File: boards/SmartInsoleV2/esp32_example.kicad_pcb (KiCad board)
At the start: 2 copper layers, 49 x 38.4 mm, 49 parts, among them J1 Conn_01x02_Pin, J2 USB_B_Micro, J3 Conn_01x05_Female, J4 Conn_02x10_Odd_Even, J5 Conn_01x02_Pin, J7 Conn_ARM_JTAG_SWD_10, J8 Conn_01x02_Pin, Q2 SS8050-G, Q3 SS8050-G, SW1 SW_Push, SW2 SW_Push, U1 MPU-6050, U3 TLV75801PDRV, U7 ESP32-S3-WROOM-1-N16R2

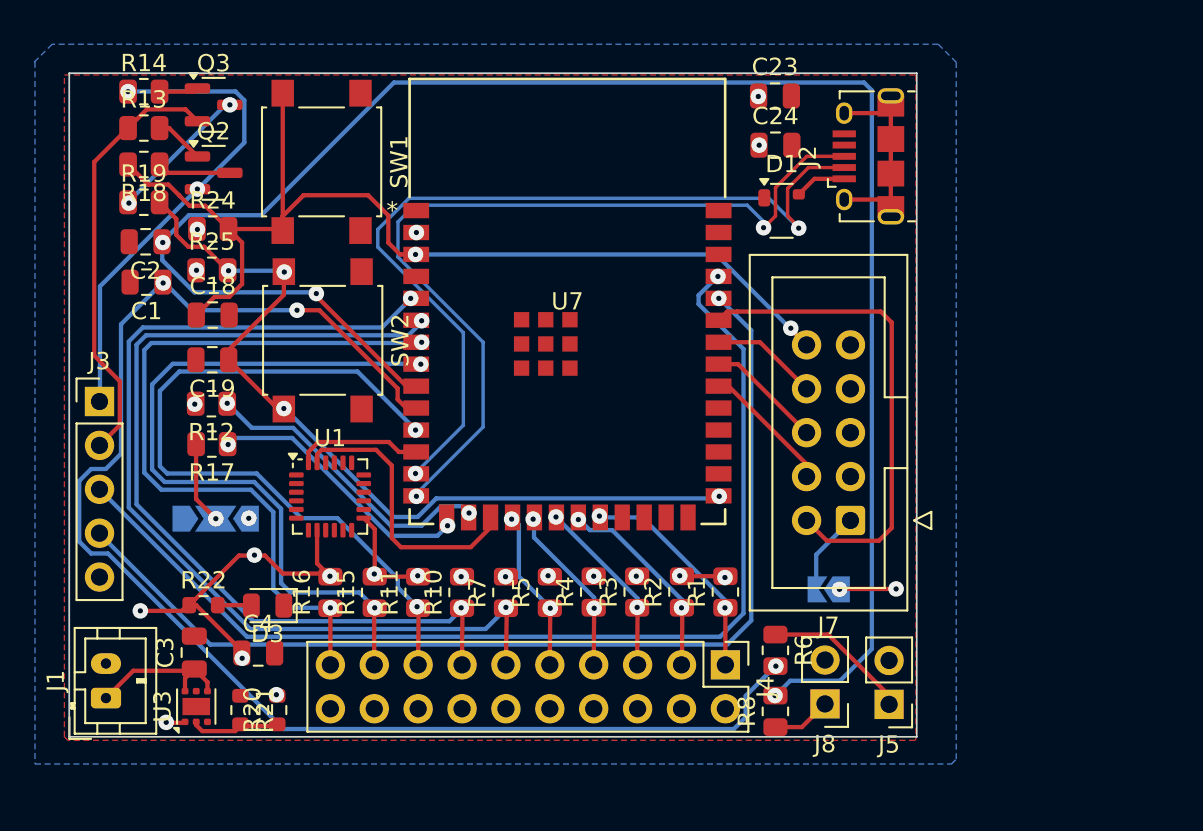
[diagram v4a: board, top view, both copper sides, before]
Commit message: 7 fine errors but need to double check the SD card footprint
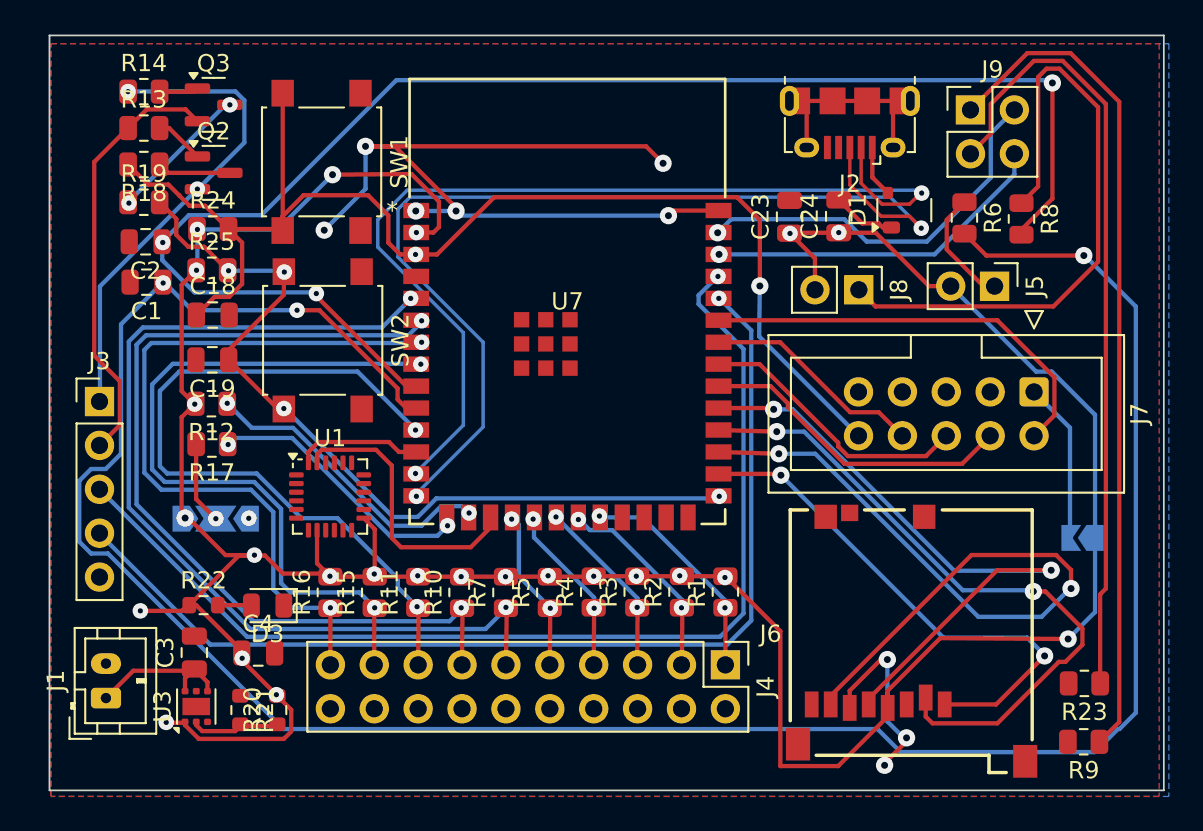
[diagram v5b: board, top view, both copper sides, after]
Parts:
- added J6: PJS008U-3000-0, MEM2051-00-195-00-A:GCT_MEM2051-00-195-00-A, F.Cu at (213.7, 73.0)
- added J9: Conn_02x02_Odd_Even, Connector_PinHeader_2.54mm:PinHeader_2x02_P2.54mm_Vertical, F.Cu at (217.1, 42.3)
- added R23: 100k, Resistor_SMD:R_0805_2012Metric, F.Cu at (223.7, 75.5)
- added R9: 100k, Resistor_SMD:R_0805_2012Metric, F.Cu at (223.7, 78.8)
- moved R8 31.9 mm to (220.1, 48.6), turned to -90 degrees
- moved R6 27.3 mm to (216.8, 48.5)
- moved J5 25.0 mm to (218.5, 52.5), turned to -90 degrees
- moved J8 24.0 mm to (210.7, 52.7), turned to -90 degrees
- moved JP1 15.0 mm to (223.6, 67.0)
- moved J7 13.0 mm to (220.8, 58.6), turned to -90 degrees
- moved D1 7.10 mm to (213.3, 48.1), turned to 90 degrees
- moved C23 7.04 mm to (206.7, 48.5), turned to 90 degrees
- moved C24 5.51 mm to (209.5, 48.4), turned to 90 degrees
- moved J2 2.19 mm to (210.2, 43.1), turned to 180 degrees
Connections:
- U7 pad 38: unconnected-(U7-IO2-Pad38) -> Net-(J9-Pin_4)
- U7 pad 39: unconnected-(U7-IO1-Pad39) -> Net-(J9-Pin_2)
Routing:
- net +3V3: track 33.3 -> 174.0 mm, vias 23 -> 24
- net GND: track 0.00 -> 63.2 mm, vias 1 -> 10
- net /End Hike: track 82.6 -> 138.1 mm
- net Net-(J9-Pin_1): track 0.00 -> 48.7 mm
- net Net-(J9-Pin_3): track 0.00 -> 45.8 mm
- net /MISO: track 0.00 -> 44.5 mm, vias 0 -> 2
- net /MOSI: track 0.00 -> 39.2 mm, vias 0 -> 2
- net /SCLK: track 0.00 -> 37.5 mm, vias 0 -> 2
- net Net-(J8-Pin_1): track 3.43 -> 36.6 mm
- net /CS: track 0.00 -> 30.6 mm, vias 0 -> 2
- net Net-(J9-Pin_2): track 0.00 -> 22.7 mm, vias 0 -> 1
- net Net-(J9-Pin_4): track 0.00 -> 20.2 mm, vias 0 -> 1
- net /Start Hike: track 103.1 -> 84.3 mm
- net /CHIP_PU: track 62.9 -> 73.7 mm
- net /MTCK: track 7.68 -> 18.4 mm
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- added copper zone on B.Cu, net GND
- removed copper zone on B.Cu, net +3V3
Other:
- board size 49 x 38.4 mm -> 64.5 x 43.7 mm

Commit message: submitted for round 5
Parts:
- added C5: 1uF, Capacitor_SMD:C_0805_2012Metric, F.Cu at (225.6, 48.7)
- added J10: Conn_01x02_Pin, Connector_PinHeader_2.54mm:PinHeader_1x02_P2.54mm_Vertical, F.Cu at (223.7, 43.0)
- added R26: 5k, Resistor_SMD:R_0805_2012Metric, F.Cu at (226.6, 44.4)
- moved J2 2.32 mm to (210.2, 40.7)
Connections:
- J1 pad 1: /POWER FROM BATTERY -> +5V
- U7 pad 24: unconnected-(U7-IO47-Pad24) -> /Bluetooth
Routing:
- net +5V: track 3.00 -> 127.7 mm
- net /Start Hike: track 84.3 -> 189.3 mm
- net /Bluetooth: track 0.00 -> 48.4 mm
- net GND: track 63.2 -> 73.1 mm, vias 10 -> 12
- net /POWER FROM BATTERY: track 8.90 -> 3.11 mm
- net Net-(J10-Pin_1): track 0.00 -> 3.78 mm
- net Net-(J9-Pin_3): track 45.8 -> 49.0 mm
- net +3V3: track 174.0 -> 177.0 mm, vias 24 -> 5
- net Net-(J9-Pin_1): track 48.7 -> 51.5 mm
- net /End Hike: track 138.1 -> 140.5 mm
- net /D+: track 59.0 -> 61.3 mm
- net /D-: track 57.1 -> 59.4 mm
- net unconnected-(J2-Shield-Pad6): track 11.5 -> 12.3 mm
- net /RTS: vias 3 -> 2
- net /RX: vias 2 -> 1
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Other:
- board size 64.5 x 43.7 mm -> 65.9 x 44 mm
- board text added: "Smart Insole - Team 41 - 2024/04/09"
